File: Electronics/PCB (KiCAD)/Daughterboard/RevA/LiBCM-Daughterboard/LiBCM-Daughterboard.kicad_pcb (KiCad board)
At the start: 4 copper layers, 113.7 x 80.8 mm, 0 parts

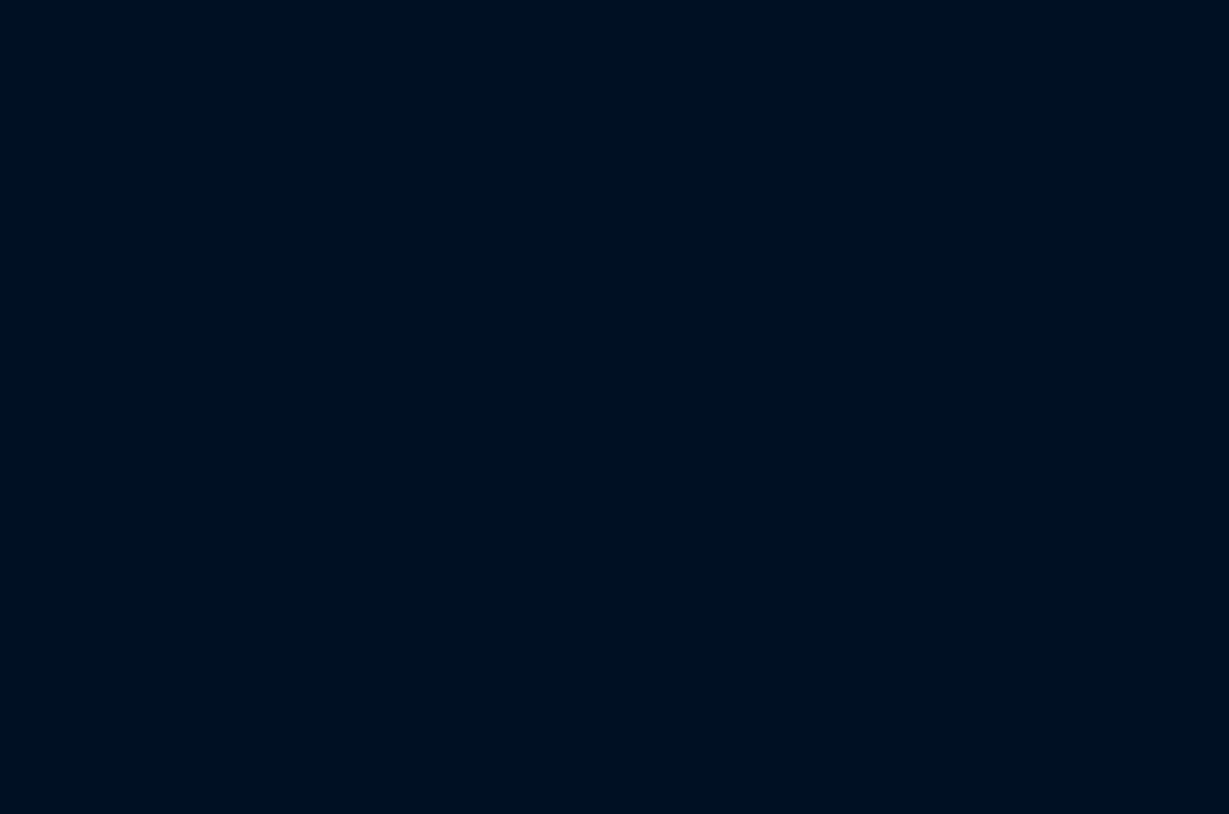
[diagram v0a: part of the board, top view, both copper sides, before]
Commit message: RevB Heater PCBs, Daughterboard Schematic
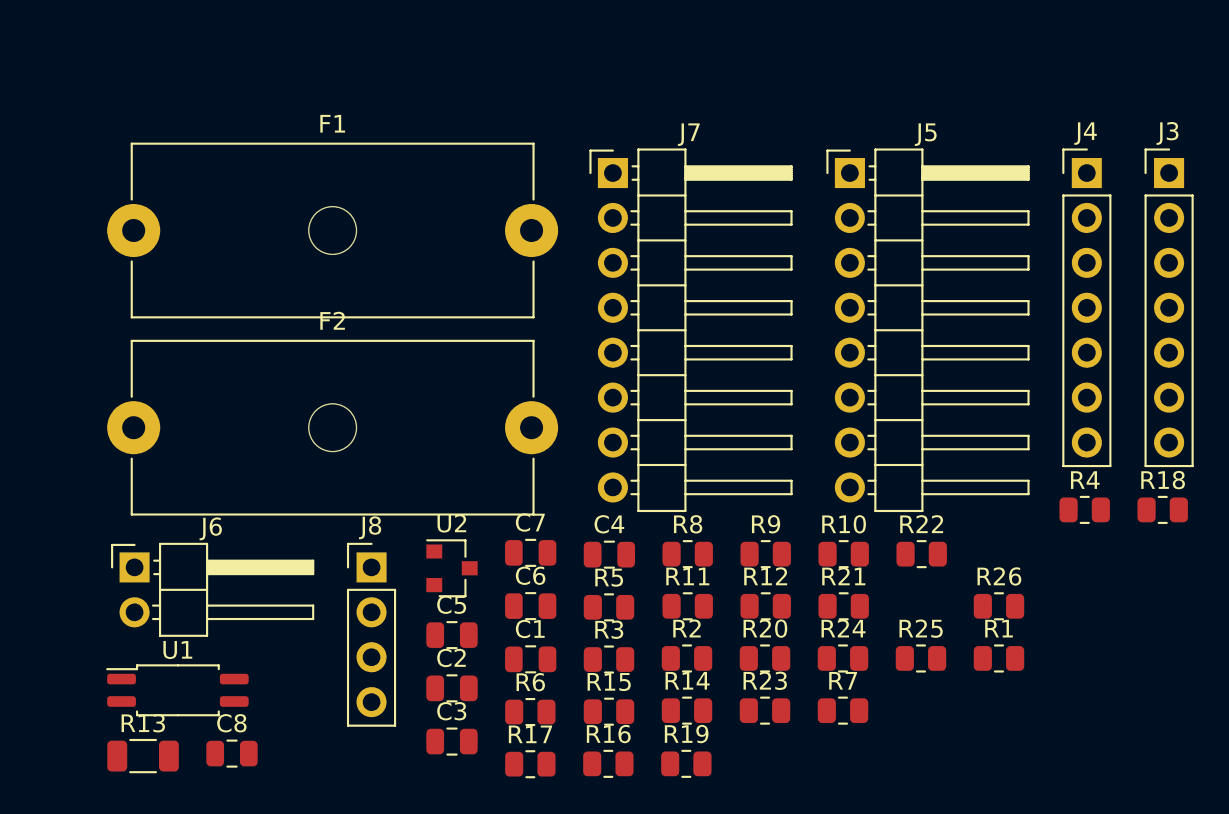
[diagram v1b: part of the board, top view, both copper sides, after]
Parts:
- added C1: 100n, Capacitor_SMD:C_0805_2012Metric, F.Cu at (184.5, 200.3)
- added C2: 100n, Capacitor_SMD:C_0805_2012Metric, F.Cu at (180.0, 202.0)
- added C3: 100n, Capacitor_SMD:C_0805_2012Metric, F.Cu at (180.0, 205.0)
- added C4: 100n, Capacitor_SMD:C_0805_2012Metric, F.Cu at (188.9, 194.4)
- added C5: 100n, Capacitor_SMD:C_0805_2012Metric, F.Cu at (180.0, 199.0)
- added C6: 1u, Capacitor_SMD:C_0805_2012Metric, F.Cu at (184.5, 197.3)
- added C7: 100n, Capacitor_SMD:C_0805_2012Metric, F.Cu at (184.5, 194.3)
- added C8: 100n, Capacitor_SMD:C_0805_2012Metric, F.Cu at (167.6, 205.7)
- added F1: Fuse, Fuse:Fuseholder_Cylinder-5x20mm_Schurter_0031_8201_Horizontal_Open, F.Cu at (162.0, 176.1)
- added F2: Fuse, Fuse:Fuseholder_Cylinder-5x20mm_Schurter_0031_8201_Horizontal_Open, F.Cu at (162.0, 187.2)
- added J3: Conn_01x07, Connector_PinHeader_2.54mm:PinHeader_1x07_P2.54mm_Vertical, F.Cu at (220.6, 172.8)
- added J4: Conn_01x07, Connector_PinHeader_2.54mm:PinHeader_1x07_P2.54mm_Vertical, F.Cu at (215.9, 172.8)
- added J5: Conn_01x08, Connector_PinHeader_2.54mm:PinHeader_1x08_P2.54mm_Horizontal, F.Cu at (202.5, 172.8)
- added J6: Conn_01x02, Connector_PinHeader_2.54mm:PinHeader_1x02_P2.54mm_Horizontal, F.Cu at (162.1, 195.1)
- added J7: Conn_01x08, Connector_PinHeader_2.54mm:PinHeader_1x08_P2.54mm_Horizontal, F.Cu at (189.1, 172.8)
- added J8: Conn_01x04, Connector_PinHeader_2.54mm:PinHeader_1x04_P2.54mm_Vertical, F.Cu at (175.5, 195.1)
- added R1: 7k32, Resistor_SMD:R_0805_2012Metric, F.Cu at (211.0, 200.3)
- added R10: 100, Resistor_SMD:R_0805_2012Metric, F.Cu at (202.2, 194.4)
- added R11: 20, Resistor_SMD:R_0805_2012Metric, F.Cu at (193.4, 197.3)
- added R12: 100, Resistor_SMD:R_0805_2012Metric, F.Cu at (197.8, 197.3)
- added R13: 5M1, Resistor_SMD:R_1206_3216Metric, F.Cu at (162.6, 205.8)
- added R14: 100k, Resistor_SMD:R_0805_2012Metric, F.Cu at (193.3, 203.2)
- added R15: 100k, Resistor_SMD:R_0805_2012Metric, F.Cu at (188.9, 203.3)
- added R16: 100k, Resistor_SMD:R_0805_2012Metric, F.Cu at (188.9, 206.2)
- added R17: 100k, Resistor_SMD:R_0805_2012Metric, F.Cu at (184.5, 206.3)
- added R18: 10k, Resistor_SMD:R_0805_2012Metric, F.Cu at (220.2, 191.9)
- added R19: DNP, Resistor_SMD:R_0805_2012Metric, F.Cu at (193.3, 206.2)
- added R2: 7k32, Resistor_SMD:R_0805_2012Metric, F.Cu at (193.3, 200.3)
- added R20: DNP, Resistor_SMD:R_0805_2012Metric, F.Cu at (197.7, 200.3)
- added R21: DNP, Resistor_SMD:R_0805_2012Metric, F.Cu at (202.2, 197.3)
- added R22: DNP, Resistor_SMD:R_0805_2012Metric, F.Cu at (206.6, 194.4)
- added R23: 768, Resistor_SMD:R_0805_2012Metric, F.Cu at (197.7, 203.2)
- added R24: 10k, Resistor_SMD:R_0805_2012Metric, F.Cu at (202.1, 200.3)
- added R25: 768, Resistor_SMD:R_0805_2012Metric, F.Cu at (206.5, 200.3)
- added R26: DNP, Resistor_SMD:R_0805_2012Metric, F.Cu at (211.0, 197.3)
- added R3: 7k32, Resistor_SMD:R_0805_2012Metric, F.Cu at (188.9, 200.3)
- added R4: 7k32, Resistor_SMD:R_0805_2012Metric, F.Cu at (215.8, 191.9)
- added R5: 10k, Resistor_SMD:R_0805_2012Metric, F.Cu at (188.9, 197.4)
- added R6: 10k, Resistor_SMD:R_0805_2012Metric, F.Cu at (184.5, 203.3)
- added R7: 10k, Resistor_SMD:R_0805_2012Metric, F.Cu at (202.1, 203.2)
- added R8: 768, Resistor_SMD:R_0805_2012Metric, F.Cu at (193.4, 194.4)
- added R9: 768, Resistor_SMD:R_0805_2012Metric, F.Cu at (197.8, 194.4)
- added U1: APV1121S, Package_SO:SOP-4_4.4x2.6mm_P1.27mm, F.Cu at (164.5, 202.1)
- added U2: LM4040DBZ-5, Package_TO_SOT_SMD:SOT-23, F.Cu at (180.0, 195.2)
